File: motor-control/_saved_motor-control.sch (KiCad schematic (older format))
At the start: 10 parts, among them P1 CONN_02X12, P2 to_motor_phase_1, P3 to_motor_phase_2, P4 to_motor_phase_3, P5 CONN_01X01, P6 CONN_01X01, P7 CONN_01X04, U5 ADT7301

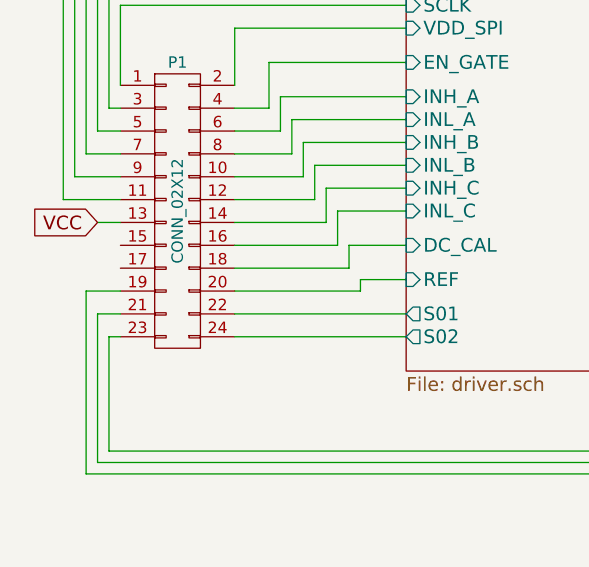
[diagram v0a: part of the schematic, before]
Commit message: Modified power layout extensively, moved vcc pin
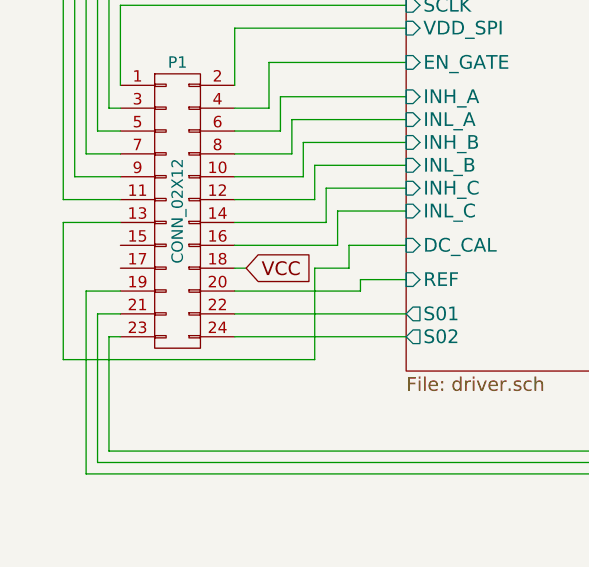
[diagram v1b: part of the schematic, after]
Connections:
- net Gate-Driver/DC_CAL: now also P1.13 (P13); no longer P1.18 (P18)
- net VCC: now also P1.18 (P18); no longer P1.13 (P13)
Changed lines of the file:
@@
 	3950 3850 3950 3950
-Wire Wire Line
-	3950 3950 3450 3950
 Wire Wire Line
 	4200 3700 3900 3700
@@
 	10650 5450 10650 5350
 Connection ~ 10650 5350
-Text GLabel 2850 3750 0    60   Input ~ 0
+Text GLabel 3500 3950 2    60   Input ~ 0
 VCC
-Wire Wire Line
-	2850 3750 2950 3750
 $Comp
 L ADT7301 U5
@@
 Wire Wire Line
 	5150 5450 5350 5450
+Wire Wire Line
+	3500 3950 3450 3950
+Wire Wire Line
+	3950 3950 3800 3950
+Wire Wire Line
+	3800 3950 3800 4350
+Wire Wire Line
+	3800 4350 2700 4350
+Wire Wire Line
+	2700 4350 2700 3750
+Wire Wire Line
+	2700 3750 2950 3750
 $EndSCHEMATC
